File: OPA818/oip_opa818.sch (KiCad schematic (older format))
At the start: 35 parts, among them J101 Conn_Coaxial, J102 Conn_01x03, U101 LT3042xMSE, U102 LT3093xMSE, U103 OPA818IDRGx, U104 BUF602xDBV

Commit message: add bom
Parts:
- removed C110, C111: C, Capacitor_SMD:C_0402_1005Metric, symbol Device:C
- U103: symbol aw:OPA818IDRGx -> oip_opa818-rescue:OPA818IDRGx-aw
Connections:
- wire segments 116 -> 112
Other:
- note added: "OPA818 max supply voltage 13V\nuse e.g. +V=+6V and -V=-6V"
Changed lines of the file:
@@
 R1 10R or 20R
 $Comp
-L aw:OPA818IDRGx U103
+L oip_opa818-rescue:OPA818IDRGx-aw U103
 U 1 1 5F1643B5
 P 4700 3050
@@
 	5550 3050 5500 3050
 NoConn ~ 5850 3350
-$Comp
-L Device:C C111
-U 1 1 5F185FBF
-P 4950 1850
-F 0 "C111" H 4950 1950 50  0000 L CNN
-F 1 "C" H 4850 1750 50  0000 L CNN
-F 2 "Capacitor_SMD:C_0402_1005Metric" H 4988 1700 50  0001 C CNN
-F 3 "~" H 4950 1850 50  0001 C CNN
-	1    4950 1850
-	0    1    1    0
-$EndComp
-$Comp
-L Device:C C110
-U 1 1 5F1863B8
-P 4750 1650
-F 0 "C110" H 4800 1550 50  0000 L CNN
-F 1 "C" H 4650 1550 50  0000 L CNN
-F 2 "Capacitor_SMD:C_0402_1005Metric" H 4788 1500 50  0001 C CNN
-F 3 "~" H 4750 1650 50  0001 C CNN
-	1    4750 1650
-	-1   0    0    1
-$EndComp
-Wire Wire Line
-	4800 1850 4750 1850
-Wire Wire Line
-	4750 1800 4750 1850
-Connection ~ 4750 1850
-Wire Wire Line
-	4750 1850 4700 1850
 Wire Wire Line
 	4400 1850 4350 1850
-Wire Wire Line
-	5100 1850 5250 1850
-$Comp
-L power:GND #PWR0121
-U 1 1 5F194372
-P 4750 1450
-F 0 "#PWR0121" H 4750 1200 50  0001 C CNN
-F 1 "GND" H 4755 1277 50  0000 C CNN
-F 2 "" H 4750 1450 50  0001 C CNN
-F 3 "" H 4750 1450 50  0001 C CNN
-	1    4750 1450
-	-1   0    0    1
-$EndComp
-Wire Wire Line
-	4750 1450 4750 1500
 $Bitmap
 Pos 4850 850
@@
 EndData
 $EndBitmap
+Wire Wire Line
+	4700 1850 5250 1850
+Text Notes 4300 5700 0    50   ~ 0
+OPA818 max supply voltage 13V\nuse e.g. +V=+6V and -V=-6V
 $EndSCHEMATC

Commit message: OPA818 notes
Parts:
- U103: symbol oip_opa818-rescue:OPA818IDRGx-aw -> oip_opa818-rescue:OPA818IDRGx-aw-oip_opa818-rescue
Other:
- note added: "TIASim predictions (https://github.com/aewallin/TIASim)\n\nFast detector:\nDiode FDS015, RF 1.2 kOhm, CF 0.6 pF gives BW-3dB: 452 MHz\n\nSlow detector: \nDiode S5973, RF 1 MOhm, CF None, BW-3db: 3.5 MHz\n"

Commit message: add notes
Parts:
- R101, R107: value 25k -> 56k
- U103: symbol oip_opa818-rescue:OPA818IDRGx-aw-oip_opa818-rescue -> oip_opa818-rescue:OPA818IDRGx-aw-oip_opa818-rescue-oip_opa818-rescue
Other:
- note added: "12" MMCX-to-SMA lead, RG316\nDigikey 744-1700-ND"
- note added: "Digikey WM5557-ND"
- note added: "Lead colors\nBrown (+12V)\nBlack (GND)\nBlue (-12V)"
- note added: "Measured\n+5.57 V"
- note added: "Measured\n-5.59 V"
- note added: "OPA818 max supply voltage 13V\nuse e.g. +V=+6V and -V=-6V\n\nBUF602 max +/- 6.5 V"
- note added: "PSU:\nThorlabs LDS12B\n±12 VDC Regulated Linear Power Supply, 6 W\nLumberg RSMV3 male connector, 3-pin\n\nPSU-lead: Digikey A120947-ND (mates with Thorlabs 3-pin psu connector)\n3-pin M8 female connector\n1.5 m 3-wire lead, solder to PCB"
- note added: "Photodiodes with TO-18 footprint:\n\nFarnell 1495575\nHamamatsu S5973\nD= 400um active area\nCd=1.6 pF @ Vr=3V3\n\nThorlabs FDS015\nD=150 um active area\n0.65pF @ Vr = 5 V\n\nThorlabs FDS025\nD= 250 um active area, with ball lens\n0.94 pF @ Vr = 5 V\n\nHamamatsu S5972\nD= 800um active area\n3 pF @ Vr = 10 V\n\nHamamatsu S5971\nD= 1.2 mm active area\n3 pF @ Vr = 10 V\n\n\nOSI FCI-125G-006HRL\nHama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"
- note added: "option:\nDC-coupling with \n0-10R resistor here?"
- note removed: "12" MMCX-to-SMA lead, RG316\n744-1700-ND"
- note removed: "1495575\nHamamatsu S5973\nCd=1p6 F @ Vr=3V3"
- note removed: "Alternative photodiodes\nOSI FCI-125G-006HRL\nHamamatsu S9055(-01)\nThorlabs FDS015, FDS025"
- note removed: "OPA818 max supply voltage 13V\nuse e.g. +V=+6V and -V=-6V"
- note removed: "WM5557-ND"
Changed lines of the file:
@@
 P 2900 5250
 F 0 "R101" H 2970 5296 50  0000 L CNN
-F 1 "25k" H 2970 5205 50  0000 L CNN
+F 1 "56k" V 2900 5150 50  0000 L CNN
 F 2 "Resistor_SMD:R_0603_1608Metric" V 2830 5250 50  0001 C CNN
 F 3 "~" H 2900 5250 50  0001 C CNN
@@
 P 2950 6100
 F 0 "R107" H 3020 6146 50  0000 L CNN
-F 1 "25k" H 3020 6055 50  0000 L CNN
+F 1 "56k" V 2950 6000 50  0000 L CNN
 F 2 "Resistor_SMD:R_0603_1608Metric" V 2880 6100 50  0001 C CNN
 F 3 "~" H 2950 6100 50  0001 C CNN
@@
 Wire Wire Line
 	4200 6700 4450 6700
-Text Notes 2150 3000 0    50   ~ 0
-1495575\nHamamatsu S5973\nCd=1p6 F @ Vr=3V3
 Text Notes 3150 4350 0    50   ~ 0
 LT3042EMSE#PBF-ND
@@
 LT3093EMSE#PBF-ND
 Text Notes 7100 3300 0    50   ~ 0
-WM5557-ND
+Digikey WM5557-ND
 Text Notes 7850 3100 0    50   ~ 0
-12" MMCX-to-SMA lead, RG316\n744-1700-ND
+12" MMCX-to-SMA lead, RG316\nDigikey 744-1700-ND
 Text Label 1650 6100 0    50   ~ 0
 -VIN
@@
 Text Notes 10250 6400 0    50   ~ 0
 Open Hardware
-Text Notes 1100 2400 0    50   ~ 0
-Alternative photodiodes\nOSI FCI-125G-006HRL\nHamamatsu S9055(-01)\nThorlabs FDS015, FDS025
+Text Notes 700  2900 0    50   ~ 0
+Photodiodes with TO-18 footprint:\n\nFarnell 1495575\nHamamatsu S5973\nD= 400um active area\nCd=1.6 pF @ Vr=3V3\n\nThorlabs FDS015\nD=150 um active area\n0.65pF @ Vr = 5 V\n\nThorlabs FDS025\nD= 250 um active area, with ball lens\n0.94 pF @ Vr = 5 V\n\nHamamatsu S5972\nD= 800um active area\n3 pF @ Vr = 10 V\n\nHamamatsu S5971\nD= 1.2 mm active area\n3 pF @ Vr = 10 V\n\n\nOSI FCI-125G-006HRL\nHamamatsu S9055(-01)\n
 $Comp
 L Connector:TestPoint TP102
@@
 R1 10R or 20R
 $Comp
-L oip_opa818-rescue:OPA818IDRGx-aw-oip_opa818-rescue U103
+L oip_opa818-rescue:OPA818IDRGx-aw-oip_opa818-rescue-oip_opa818-rescue U103
 U 1 1 5F1643B5
 P 4700 3050
@@
 	4700 1850 5250 1850
 Text Notes 4300 5700 0    50   ~ 0
-OPA818 max supply voltage 13V\nuse e.g. +V=+6V and -V=-6V
+OPA818 max supply voltage 13V\nuse e.g. +V=+6V and -V=-6V\n\nBUF602 max +/- 6.5 V
 Text Notes 4550 1250 0    50   ~ 0
 TIASim predictions (https://github.com/aewallin/TIASim)\n\nFast detector:\nDiode FDS015, RF 1.2 kOhm, CF 0.6 pF gives BW-3dB: 452 MHz\n\nSlow detector: \nDiode S5973, RF 1 MOhm, CF None, BW-3db: 3.5 MHz\n
+Text Notes 500  5700 0    50   ~ 0
+Lead colors\nBrown (+12V)\nBlack (GND)\nBlue (-12V)
+Text Notes 4600 4700 0    50   ~ 0
+Measured\n+5.57 V
+Text Notes 4550 6700 0    50   ~ 0
+Measured\n-5.59 V
+Text Notes 700  4400 0    50   ~ 0
+PSU:\nThorlabs LDS12B\n±12 VDC Regulated Linear Power Supply, 6 W\nLumberg RSMV3 male connector, 3-pin\n\nPSU-lead: Digikey A120947-ND (mates with Thorlabs 3-pin psu connector)\n3-pin M8 female connector\n1.5 m 3-wire lead, solder to PCB
+Text Notes 5100 3400 0    30   ~ 0
+option:\nDC-coupling with \n0-10R resistor here?
 $EndSCHEMATC

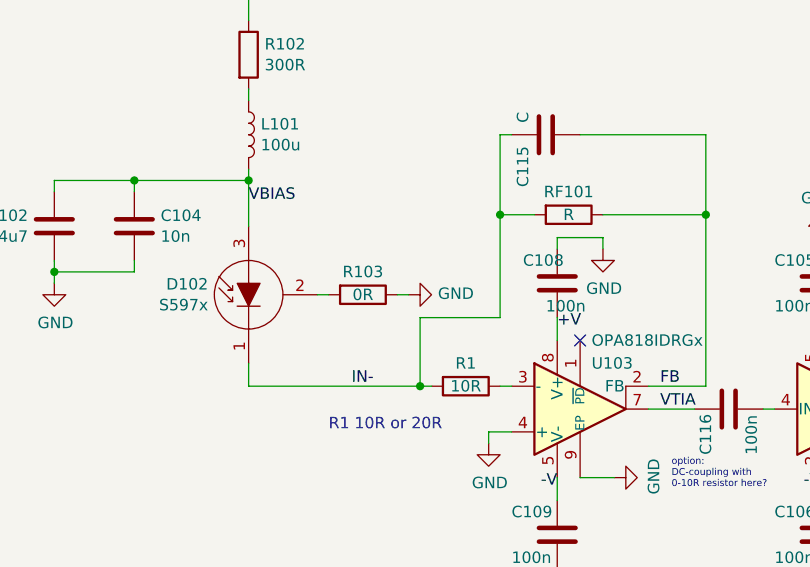
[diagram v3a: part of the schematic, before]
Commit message: move all parts to top side of pcb
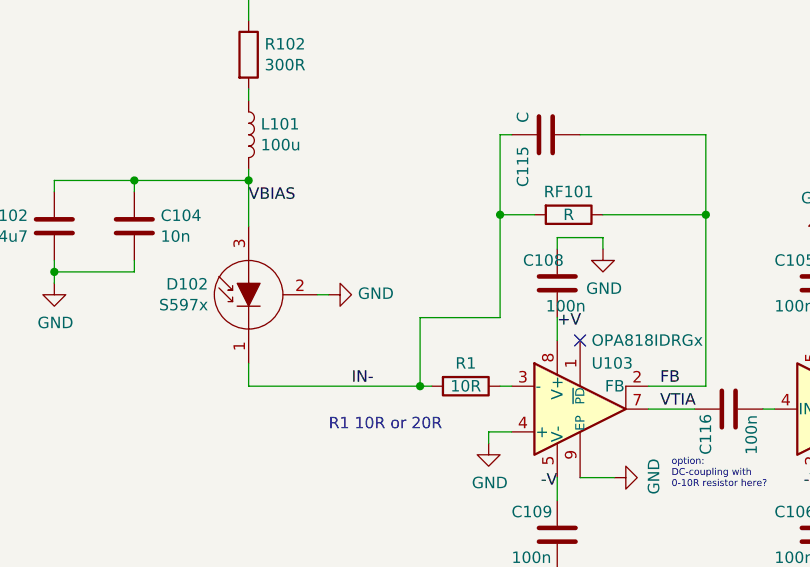
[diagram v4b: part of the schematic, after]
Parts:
- removed R103: 0R, Resistor_SMD:R_0603_1608Metric, symbol Device:R
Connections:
- net GND: now also D102.2 (C)
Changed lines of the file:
@@
-$EndComp
-$Comp
-L Device:R R103
-U 1 1 5E080F1F
-P 3750 2550
-F 0 "R103" V 3650 2550 50  0000 C CNN
-F 1 "0R" V 3750 2550 50  0000 C CNN
-F 2 "Resistor_SMD:R_0603_1608Metric" V 3680 2550 50  0001 C CNN
-F 3 "~" H 3750 2550 50  0001 C CNN
-	1    3750 2550
-	0    1    1    0
 $EndComp
 $Comp
 L power:GND #PWR0101
 U 1 1 5E0815B9
-P 3950 2550
-F 0 "#PWR0101" H 3950 2300 50  0001 C CNN
-F 1 "GND" V 3955 2422 50  0000 R CNN
-F 2 "" H 3950 2550 50  0001 C CNN
-F 3 "" H 3950 2550 50  0001 C CNN
-	1    3950 2550
+P 3600 2550
+F 0 "#PWR0101" H 3600 2300 50  0001 C CNN
+F 1 "GND" V 3605 2422 50  0000 R CNN
+F 2 "" H 3600 2550 50  0001 C CNN
+F 3 "" H 3600 2550 50  0001 C CNN
+	1    3600 2550
 	0    -1   -1   0
 $EndComp
@@
 	7000 3300 7000 3250
 Wire Wire Line
-	3950 2550 3900 2550
-Wire Wire Line
 	3600 2550 3550 2550

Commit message: add PDF docs
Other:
- note added: "MMCX connector\nDigikey WM5557-ND"
- note added: "SOD323F"
- note removed: "Digikey WM5557-ND"
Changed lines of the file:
@@
 Text Notes 3050 7200 0    50   ~ 0
 LT3093EMSE#PBF-ND
-Text Notes 7100 3300 0    50   ~ 0
-Digikey WM5557-ND
-Text Notes 7850 3100 0    50   ~ 0
+Text Notes 7100 2950 0    50   ~ 0
+MMCX connector\nDigikey WM5557-ND
+Text Notes 8050 2950 0    50   ~ 0
 12" MMCX-to-SMA lead, RG316\nDigikey 744-1700-ND
 Text Label 1650 6100 0    50   ~ 0
@@
 Text Notes 5100 3400 0    30   ~ 0
 option:\nDC-coupling with \n0-10R resistor here?
+Text Notes 1900 4900 0    50   ~ 0
+SOD323F
 $EndSCHEMATC

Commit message: docs
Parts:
- U103: symbol oip_opa818-rescue:OPA818IDRGx-aw-oip_opa818-rescue-oip_opa818-rescue -> oip_opa818-rescue:OPA818IDRGx-aw-oip_opa818-rescue-oip_opa818-rescue-oip_opa818-rescue
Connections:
- net VBIAS renamed -5VBIAS
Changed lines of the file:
@@
 $EndComp
 Text Label 3250 2150 0    50   ~ 0
-VBIAS
+-5VBIAS
 Text Label 5050 3050 0    50   ~ 0
 VTIA
@@
 R1 10R or 20R
 $Comp
-L oip_opa818-rescue:OPA818IDRGx-aw-oip_opa818-rescue-oip_opa818-rescue U103
+L oip_opa818-rescue:OPA818IDRGx-aw-oip_opa818-rescue-oip_opa818-rescue-oip_opa818-rescue U103
 U 1 1 5F1643B5
 P 4700 3050
